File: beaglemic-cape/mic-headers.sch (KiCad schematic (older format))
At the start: 28 parts, among them J10 MIC-04, J11 MIC-06, J12 MIC-08, J13 MIC-10, J14 MIC-12, J15 MIC-14, J16 MIC-01, J17 MIC-03, J18 MIC-05, J19 MIC-07, J20 MIC-09, J21 MIC-11, J22 MIC-13, J23 MIC-15, J8 MIC-00, J9 MIC-02, U4 74HCT244, U5 SPM0423HD4H-WB, U6 SPM0423HD4H-WB

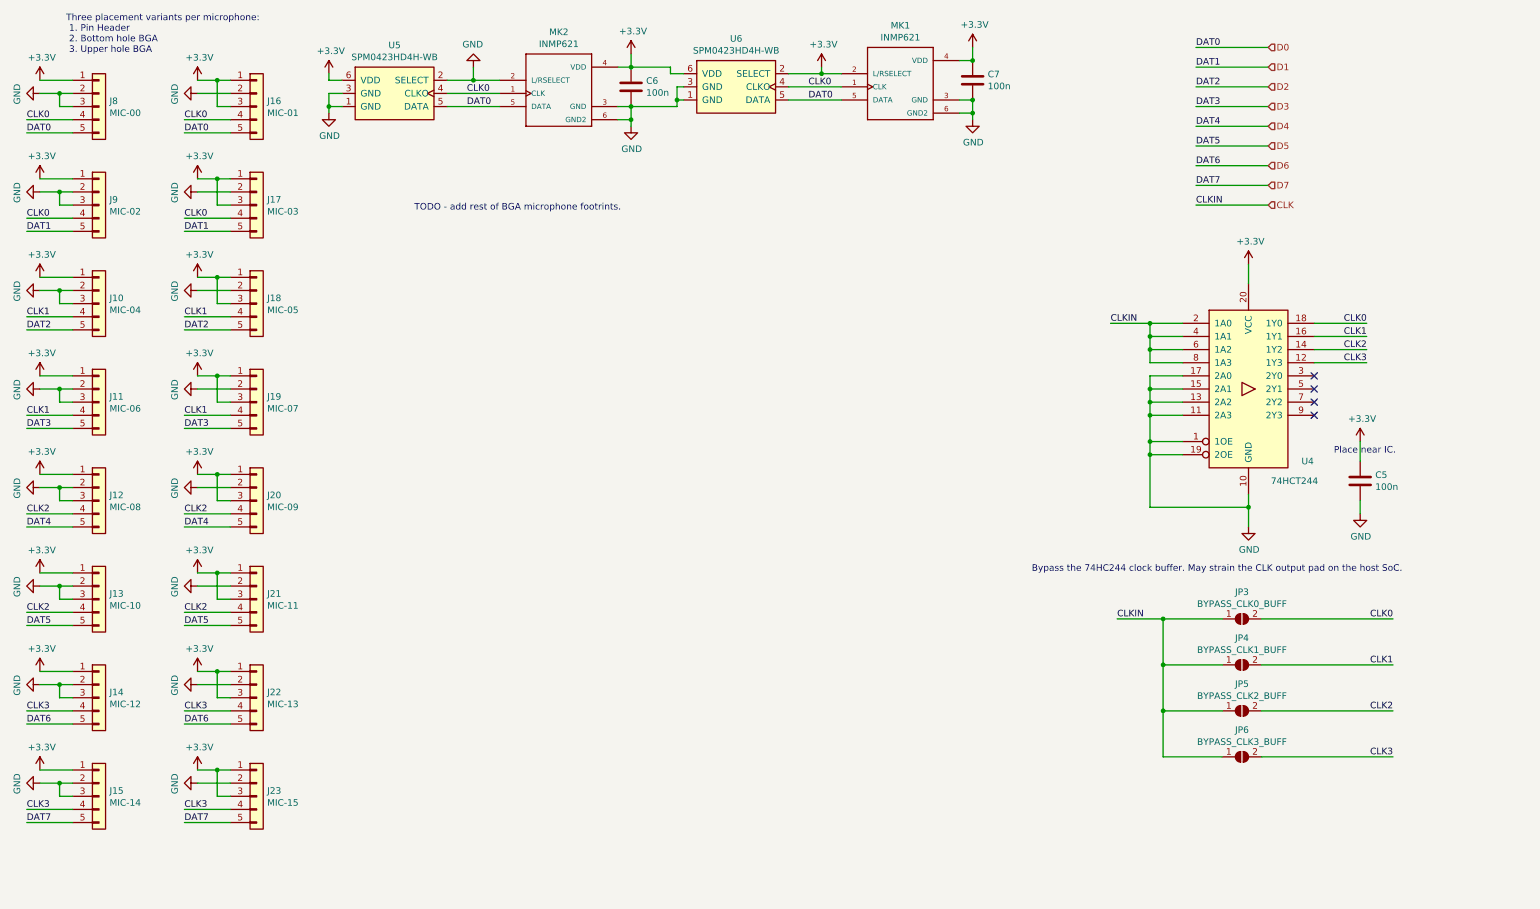
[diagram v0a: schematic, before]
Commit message: beaglemic-cape: Shrink PCB to 100x100mm
Let's keep the PCB in the hobby price range.

Version 1.0-rc2

TODO: Route me!

Signed-off-by: Dimitar Dimitrov <dimitar@dinux.eu>
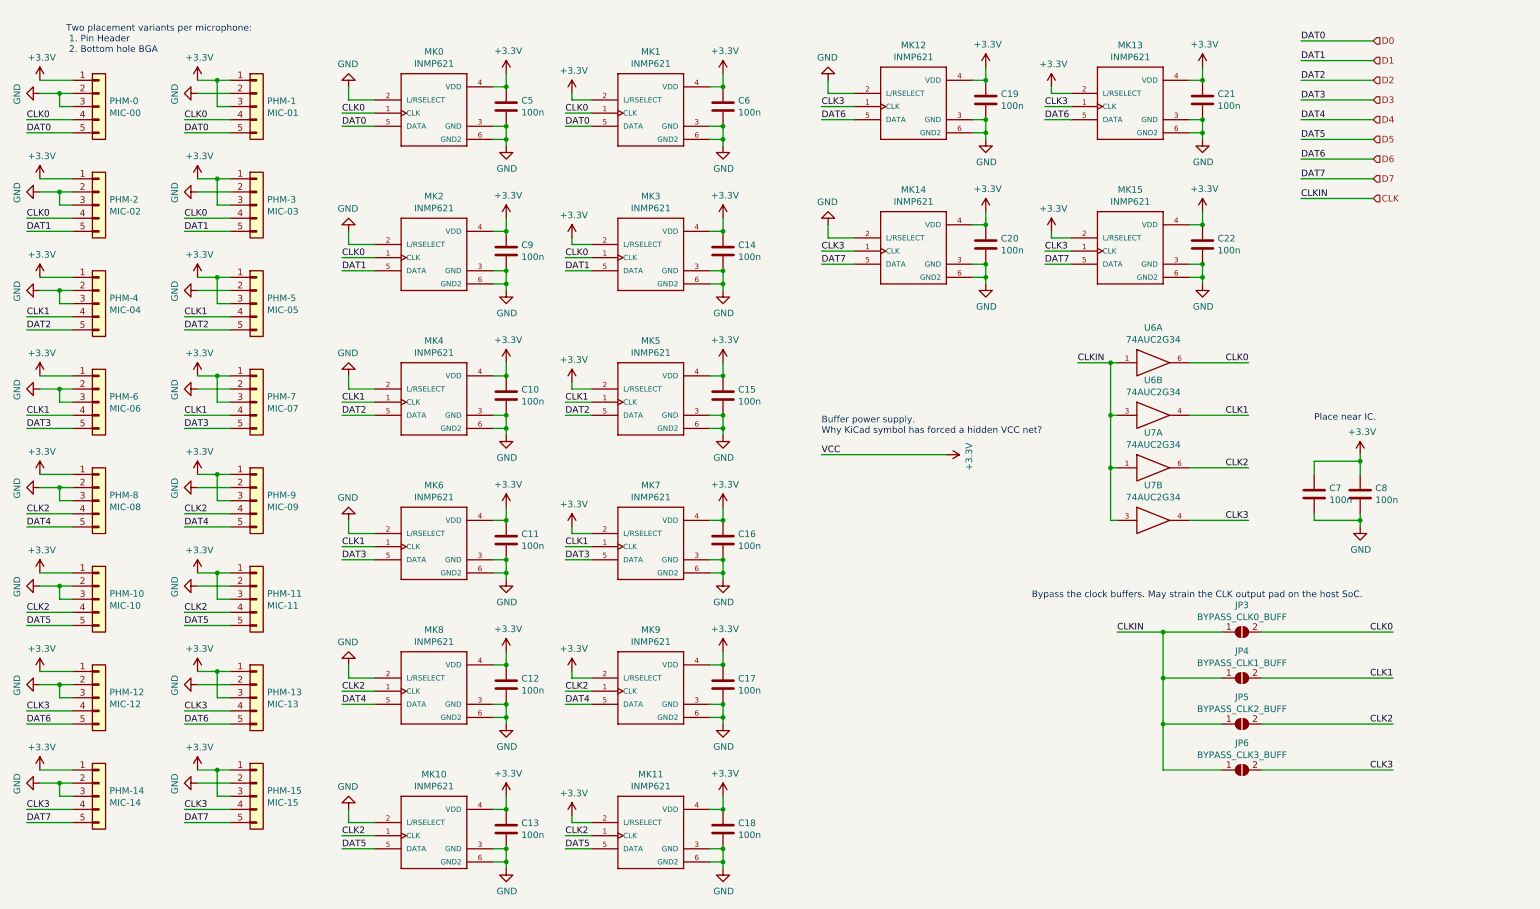
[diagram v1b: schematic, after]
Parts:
- removed U4: 74HCT244, Package_SO:TSSOP-20_4.4x6.5mm_P0.65mm, symbol 74xx:74HCT244
- removed U5, U6: SPM0423HD4H-WB, bga-6:BGA_6, symbol digital-mics:SPM0423HD4H-WB
- added C10, C11, C12, C13, C14, C15, C16, C17, C18, C19, C20, C21, C22, C7, C9: 100n, Capacitor_SMD:C_0805_2012Metric, symbol Device:C
- added MK10, MK11, MK12, MK13, MK14, MK15, MK2, MK3, MK4, MK5, MK6, MK7, MK8, MK9: INMP621, inmp621-footprint:MK_INMP621, symbol INMP621:INMP621
- added U6, U7: 74AUC2G34, Package_TO_SOT_SMD:SOT-23-6, symbol 74xGxx:74AUC2G34
- PHM-0: renamed from J8; footprint Connector_PinSocket_2.54mm:PinSocket_1x05_P2.54mm_Horizontal -> pinheader-smd:pinheader-5-smd-pads
- PHM-1: renamed from J16; footprint Connector_PinSocket_2.54mm:PinSocket_1x05_P2.54mm_Horizontal -> pinheader-smd:pinheader-5-smd-pads
- PHM-10: renamed from J13; footprint Connector_PinSocket_2.54mm:PinSocket_1x05_P2.54mm_Horizontal -> pinheader-smd:pinheader-5-smd-pads
- PHM-11: renamed from J21; footprint Connector_PinSocket_2.54mm:PinSocket_1x05_P2.54mm_Horizontal -> pinheader-smd:pinheader-5-smd-pads
- PHM-12: renamed from J14; footprint Connector_PinSocket_2.54mm:PinSocket_1x05_P2.54mm_Horizontal -> pinheader-smd:pinheader-5-smd-pads
- PHM-13: renamed from J22; footprint Connector_PinSocket_2.54mm:PinSocket_1x05_P2.54mm_Horizontal -> pinheader-smd:pinheader-5-smd-pads
- PHM-14: renamed from J15; footprint Connector_PinSocket_2.54mm:PinSocket_1x05_P2.54mm_Horizontal -> pinheader-smd:pinheader-5-smd-pads
- PHM-15: renamed from J23; footprint Connector_PinSocket_2.54mm:PinSocket_1x05_P2.54mm_Horizontal -> pinheader-smd:pinheader-5-smd-pads
- PHM-2: renamed from J9; footprint Connector_PinSocket_2.54mm:PinSocket_1x05_P2.54mm_Horizontal -> pinheader-smd:pinheader-5-smd-pads
- PHM-3: renamed from J17; footprint Connector_PinSocket_2.54mm:PinSocket_1x05_P2.54mm_Horizontal -> pinheader-smd:pinheader-5-smd-pads
- PHM-4: renamed from J10; footprint Connector_PinSocket_2.54mm:PinSocket_1x05_P2.54mm_Horizontal -> pinheader-smd:pinheader-5-smd-pads
- PHM-5: renamed from J18; footprint Connector_PinSocket_2.54mm:PinSocket_1x05_P2.54mm_Horizontal -> pinheader-smd:pinheader-5-smd-pads
- PHM-6: renamed from J11; footprint Connector_PinSocket_2.54mm:PinSocket_1x05_P2.54mm_Horizontal -> pinheader-smd:pinheader-5-smd-pads
- PHM-7: renamed from J19; footprint Connector_PinSocket_2.54mm:PinSocket_1x05_P2.54mm_Horizontal -> pinheader-smd:pinheader-5-smd-pads
- PHM-8: renamed from J12; footprint Connector_PinSocket_2.54mm:PinSocket_1x05_P2.54mm_Horizontal -> pinheader-smd:pinheader-5-smd-pads
- PHM-9: renamed from J20; footprint Connector_PinSocket_2.54mm:PinSocket_1x05_P2.54mm_Horizontal -> pinheader-smd:pinheader-5-smd-pads
- renumbered C6 to C5, C7 to C6, C5 to C8, MK2 to MK0
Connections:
- net +3V3: now also C10.1, C11.1, C12.1, C13.1, C14.1, C15.1, C16.1, C17.1, C18.1, C19.1, C20.1, C21.1, C22.1, C7.1, C9.1, MK10.4 (VDD), MK11.2 (L/RSELECT), MK11.4 (VDD), MK12.4 (VDD), MK13.2 (L/RSELECT), MK13.4 (VDD), MK14.4 (VDD), MK15.2 (L/RSELECT), MK15.4 (VDD), MK2.4 (VDD), MK3.2 (L/RSELECT), MK3.4 (VDD), MK4.4 (VDD), MK5.2 (L/RSELECT), MK5.4 (VDD), MK6.4 (VDD), MK7.2 (L/RSELECT), MK7.4 (VDD), MK8.4 (VDD), MK9.2 (L/RSELECT), MK9.4 (VDD), U6.5 (VCC), U6.5 (VCC), U7.5 (VCC), U7.5 (VCC)
- net CLK: now also U6.1, U6.3, U7.1, U7.3
- net CLK0: now also MK2.1 (CLK), MK3.1 (CLK), U6.6
- net CLK1: now also MK4.1 (CLK), MK5.1 (CLK), MK6.1 (CLK), MK7.1 (CLK), U6.4
- net CLK2: now also MK10.1 (CLK), MK11.1 (CLK), MK8.1 (CLK), MK9.1 (CLK), U7.6
- net CLK3: now also MK12.1 (CLK), MK13.1 (CLK), MK14.1 (CLK), MK15.1 (CLK), U7.4
- net D1: now also MK2.5 (DATA), MK3.5 (DATA)
- net D2: now also MK4.5 (DATA), MK5.5 (DATA)
- net D3: now also MK6.5 (DATA), MK7.5 (DATA)
- net D4: now also MK8.5 (DATA), MK9.5 (DATA)
- net D5: now also MK10.5 (DATA), MK11.5 (DATA)
- net D6: now also MK12.5 (DATA), MK13.5 (DATA)
- net D7: now also MK14.5 (DATA), MK15.5 (DATA)
- net GND: now also C10.2, C11.2, C12.2, C13.2, C14.2, C15.2, C16.2, C17.2, C18.2, C19.2, C20.2, C21.2, C22.2, C7.2, C9.2, MK10.2 (L/RSELECT), MK10.3 (GND), MK10.6 (GND2), MK11.3 (GND), MK11.6 (GND2), MK12.2 (L/RSELECT), MK12.3 (GND), MK12.6 (GND2), MK13.3 (GND), MK13.6 (GND2), MK14.2 (L/RSELECT), MK14.3 (GND), MK14.6 (GND2), MK15.3 (GND), MK15.6 (GND2), MK2.2 (L/RSELECT), MK2.3 (GND), MK2.6 (GND2), MK3.3 (GND), MK3.6 (GND2), MK4.2 (L/RSELECT), MK4.3 (GND), MK4.6 (GND2), MK5.3 (GND), MK5.6 (GND2), MK6.2 (L/RSELECT), MK6.3 (GND), MK6.6 (GND2), MK7.3 (GND), MK7.6 (GND2), MK8.2 (L/RSELECT), MK8.3 (GND), MK8.6 (GND2), MK9.3 (GND), MK9.6 (GND2), U6.2 (GND), U6.2 (GND), U7.2 (GND), U7.2 (GND)
- no-connect marks 4 -> 0
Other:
- note added: "Buffer power supply.\nWhy KiCad symbol has forced a hidden VCC net?"
- note added: "Bypass the clock buffers. May strain the CLK output pad on the host SoC."
- note added: "Two placement variants per microphone:\n 1. Pin Header\n 2. Bottom hole BGA"
- note removed: "Bypass the 74HC244 clock buffer. May strain the CLK output pad on the host SoC."
- note removed: "TODO - add rest of BGA microphone footrints."
- note removed: "Three placement variants per microphone:\n 1. Pin Header\n 2. Bottom hole BGA\n 3. Upper hole BGA"
- moved on the sheet: C5, C6, C8, JP3, JP4, JP5, JP6, MK0, MK1

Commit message: beaglemic-cape: Route PCB
WARNING - NOT TESTED YET!

Signed-off-by: Dimitar Dimitrov <dimitar@dinux.eu>
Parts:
- PHM-0, PHM-1, PHM-10, PHM-11, PHM-12, PHM-13, PHM-14, PHM-15, PHM-2, PHM-3, PHM-4, PHM-5, PHM-6, PHM-7, PHM-8, PHM-9: footprint pinheader-smd:pinheader-5-smd-pads -> Connector_PinSocket_2.54mm:PinSocket_1x05_P2.54mm_Vertical
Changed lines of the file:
@@
 Sheet 3 3
 Title "PDM Microphones"
-Date "2020-01-19"
-Rev "1.0-rc2"
+Date "2020-01-26"
+Rev "1.0-rc3"
 Comp "dimitar@dinux.eu"
 Comment1 "WARNING - NOT YET VALIDATED!"
@@
 F 0 "PHM-0" H 1330 1292 50  0000 L CNN
 F 1 "MIC-00" H 1330 1201 50  0000 L CNN
-F 2 "pinheader-smd:pinheader-5-smd-pads" H 1250 1250 50  0001 C CNN
+F 2 "Connector_PinSocket_2.54mm:PinSocket_1x05_P2.54mm_Vertical" H 1250 1250 50  0001 C CNN
 F 3 "~" H 1250 1250 50  0001 C CNN
 	1    1250 1250
@@
 F 0 "PHM-1" H 2530 1292 50  0000 L CNN
 F 1 "MIC-01" H 2530 1201 50  0000 L CNN
-F 2 "pinheader-smd:pinheader-5-smd-pads" H 2450 1250 50  0001 C CNN
+F 2 "Connector_PinSocket_2.54mm:PinSocket_1x05_P2.54mm_Vertical" H 2450 1250 50  0001 C CNN
 F 3 "~" H 2450 1250 50  0001 C CNN
 	1    2450 1250
@@
 F 0 "PHM-2" H 1330 2042 50  0000 L CNN
 F 1 "MIC-02" H 1330 1951 50  0000 L CNN
-F 2 "pinheader-smd:pinheader-5-smd-pads" H 1250 2000 50  0001 C CNN
+F 2 "Connector_PinSocket_2.54mm:PinSocket_1x05_P2.54mm_Vertical" H 1250 2000 50  0001 C CNN
 F 3 "~" H 1250 2000 50  0001 C CNN
 	1    1250 2000
@@
 F 0 "PHM-3" H 2530 2042 50  0000 L CNN
 F 1 "MIC-03" H 2530 1951 50  0000 L CNN
-F 2 "pinheader-smd:pinheader-5-smd-pads" H 2450 2000 50  0001 C CNN
+F 2 "Connector_PinSocket_2.54mm:PinSocket_1x05_P2.54mm_Vertical" H 2450 2000 50  0001 C CNN
 F 3 "~" H 2450 2000 50  0001 C CNN
 	1    2450 2000
@@
 F 0 "PHM-4" H 1330 2792 50  0000 L CNN
 F 1 "MIC-04" H 1330 2701 50  0000 L CNN
-F 2 "pinheader-smd:pinheader-5-smd-pads" H 1250 2750 50  0001 C CNN
+F 2 "Connector_PinSocket_2.54mm:PinSocket_1x05_P2.54mm_Vertical" H 1250 2750 50  0001 C CNN
 F 3 "~" H 1250 2750 50  0001 C CNN
 	1    1250 2750
@@
 F 0 "PHM-5" H 2530 2792 50  0000 L CNN
 F 1 "MIC-05" H 2530 2701 50  0000 L CNN
-F 2 "pinheader-smd:pinheader-5-smd-pads" H 2450 2750 50  0001 C CNN
+F 2 "Connector_PinSocket_2.54mm:PinSocket_1x05_P2.54mm_Vertical" H 2450 2750 50  0001 C CNN
 F 3 "~" H 2450 2750 50  0001 C CNN
 	1    2450 2750
@@
 F 0 "PHM-6" H 1330 3542 50  0000 L CNN
 F 1 "MIC-06" H 1330 3451 50  0000 L CNN
-F 2 "pinheader-smd:pinheader-5-smd-pads" H 1250 3500 50  0001 C CNN
+F 2 "Connector_PinSocket_2.54mm:PinSocket_1x05_P2.54mm_Vertical" H 1250 3500 50  0001 C CNN
 F 3 "~" H 1250 3500 50  0001 C CNN
 	1    1250 3500
@@
 F 0 "PHM-7" H 2530 3542 50  0000 L CNN
 F 1 "MIC-07" H 2530 3451 50  0000 L CNN
-F 2 "pinheader-smd:pinheader-5-smd-pads" H 2450 3500 50  0001 C CNN
+F 2 "Connector_PinSocket_2.54mm:PinSocket_1x05_P2.54mm_Vertical" H 2450 3500 50  0001 C CNN
 F 3 "~" H 2450 3500 50  0001 C CNN
 	1    2450 3500
@@
 F 0 "PHM-8" H 1330 4292 50  0000 L CNN
 F 1 "MIC-08" H 1330 4201 50  0000 L CNN
-F 2 "pinheader-smd:pinheader-5-smd-pads" H 1250 4250 50  0001 C CNN
+F 2 "Connector_PinSocket_2.54mm:PinSocket_1x05_P2.54mm_Vertical" H 1250 4250 50  0001 C CNN
 F 3 "~" H 1250 4250 50  0001 C CNN
 	1    1250 4250
@@
 F 0 "PHM-9" H 2530 4292 50  0000 L CNN
 F 1 "MIC-09" H 2530 4201 50  0000 L CNN
-F 2 "pinheader-smd:pinheader-5-smd-pads" H 2450 4250 50  0001 C CNN
+F 2 "Connector_PinSocket_2.54mm:PinSocket_1x05_P2.54mm_Vertical" H 2450 4250 50  0001 C CNN
 F 3 "~" H 2450 4250 50  0001 C CNN
 	1    2450 4250
@@
 F 0 "PHM-10" H 1330 5042 50  0000 L CNN
 F 1 "MIC-10" H 1330 4951 50  0000 L CNN
-F 2 "pinheader-smd:pinheader-5-smd-pads" H 1250 5000 50  0001 C CNN
+F 2 "Connector_PinSocket_2.54mm:PinSocket_1x05_P2.54mm_Vertical" H 1250 5000 50  0001 C CNN
 F 3 "~" H 1250 5000 50  0001 C CNN
 	1    1250 5000
@@
 F 0 "PHM-11" H 2530 5042 50  0000 L CNN
 F 1 "MIC-11" H 2530 4951 50  0000 L CNN
-F 2 "pinheader-smd:pinheader-5-smd-pads" H 2450 5000 50  0001 C CNN
+F 2 "Connector_PinSocket_2.54mm:PinSocket_1x05_P2.54mm_Vertical" H 2450 5000 50  0001 C CNN
 F 3 "~" H 2450 5000 50  0001 C CNN
 	1    2450 5000
@@
 F 0 "PHM-12" H 1330 5792 50  0000 L CNN
 F 1 "MIC-12" H 1330 5701 50  0000 L CNN
-F 2 "pinheader-smd:pinheader-5-smd-pads" H 1250 5750 50  0001 C CNN
+F 2 "Connector_PinSocket_2.54mm:PinSocket_1x05_P2.54mm_Vertical" H 1250 5750 50  0001 C CNN
 F 3 "~" H 1250 5750 50  0001 C CNN
 	1    1250 5750
@@
 F 0 "PHM-13" H 2530 5792 50  0000 L CNN
 F 1 "MIC-13" H 2530 5701 50  0000 L CNN
-F 2 "pinheader-smd:pinheader-5-smd-pads" H 2450 5750 50  0001 C CNN
+F 2 "Connector_PinSocket_2.54mm:PinSocket_1x05_P2.54mm_Vertical" H 2450 5750 50  0001 C CNN
 F 3 "~" H 2450 5750 50  0001 C CNN
 	1    2450 5750
@@
 F 0 "PHM-14" H 1330 6542 50  0000 L CNN
 F 1 "MIC-14" H 1330 6451 50  0000 L CNN
-F 2 "pinheader-smd:pinheader-5-smd-pads" H 1250 6500 50  0001 C CNN
+F 2 "Connector_PinSocket_2.54mm:PinSocket_1x05_P2.54mm_Vertical" H 1250 6500 50  0001 C CNN
 F 3 "~" H 1250 6500 50  0001 C CNN
 	1    1250 6500
@@
 F 0 "PHM-15" H 2530 6542 50  0000 L CNN
 F 1 "MIC-15" H 2530 6451 50  0000 L CNN
-F 2 "pinheader-smd:pinheader-5-smd-pads" H 2450 6500 50  0001 C CNN
+F 2 "Connector_PinSocket_2.54mm:PinSocket_1x05_P2.54mm_Vertical" H 2450 6500 50  0001 C CNN
 F 3 "~" H 2450 6500 50  0001 C CNN
 	1    2450 6500
